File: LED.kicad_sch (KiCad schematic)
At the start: 15 parts

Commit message: error check passed
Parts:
- RFB_730: value 0.1 Ohm -> 0.13 Ohm
- RFB_850: value 0.1 Ohm -> 0.13 Ohm; symbol C_Small_US:C_Small_US -> R_Small_US:R_Small_US
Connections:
- net VLED renamed VBAT_SYSTEM
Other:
- moved on the sheet: D_850

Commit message: placement finished on PCB
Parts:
- C730_BYP1, C850_BYP1, CSLOPE_730, CSLOPE_850, C_TEMP1: footprint LightFusion:C_0402_1005Metric -> LightFusion:C_0603_1608Metric
- R_TEMP_ALERT1: footprint LightFusion:R_0402_1005Metric -> LightFusion:R_0603_1608Metric
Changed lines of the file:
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@@
 		(property "Value" "10 nF"
 			(at 223.52 100.4569 0)
-			(show_name no)
-			(do_not_autoplace no)
-			(effects
-				(font
-					(size 1.27 1.27)
-				)
-				(justify left)
-			)
-		)
-		(property "Footprint" "LightFusion:C_0402_1005Metric"
+			(hide yes)
+			(show_name no)
+			(do_not_autoplace no)
+			(effects
+				(font
+					(size 1.27 1.27)
+				)
+				(justify left)
+			)
+		)
+		(property "Footprint" "LightFusion:C_0603_1608Metric"
 			(at 220.98 99.06 0)
 			(hide yes)
@@
 		(property "Value" "10 nF"
 			(at 133.35 99.1869 0)
-			(show_name no)
-			(do_not_autoplace no)
-			(effects
-				(font
-					(size 1.27 1.27)
-				)
-				(justify left)
-			)
-		)
-		(property "Footprint" "LightFusion:C_0402_1005Metric"
+			(hide yes)
+			(show_name no)
+			(do_not_autoplace no)
+			(effects
+				(font
+					(size 1.27 1.27)
+				)
+				(justify left)
+			)
+		)
+		(property "Footprint" "LightFusion:C_0603_1608Metric"
 			(at 130.81 97.79 0)
 			(hide yes)
@@
 			)
 		)
-		(property "Footprint" "LightFusion:C_0402_1005Metric"
+		(property "Footprint" "LightFusion:C_0603_1608Metric"
 			(at 137.16 124.46 0)
 			(hide yes)
@@
 		(property "Value" "4.7 uF"
 			(at 209.55 64.8969 0)
+			(hide yes)
 			(show_name no)
 			(do_not_autoplace no)
@@
 		(property "Value" "4.7 uF"
 			(at 97.79 64.8969 0)
+			(hide yes)
 			(show_name no)
 			(do_not_autoplace no)
@@
 			)
 		)
-		(property "Footprint" "LightFusion:R_0402_1005Metric"
+		(property "Footprint" "LightFusion:R_0603_1608Metric"
 			(at 125.73 114.3 0)
 			(hide yes)
@@
 		(property "Value" "100 nF"
 			(at 85.09 64.8969 0)
-			(show_name no)
-			(do_not_autoplace no)
-			(effects
-				(font
-					(size 1.27 1.27)
-				)
-				(justify left)
-			)
-		)
-		(property "Footprint" "LightFusion:C_0402_1005Metric"
+			(hide yes)
+			(show_name no)
+			(do_not_autoplace no)
+			(effects
+				(font
+					(size 1.27 1.27)
+				)
+				(justify left)
+			)
+		)
+		(property "Footprint" "LightFusion:C_0603_1608Metric"
 			(at 82.55 63.5 0)
 			(hide yes)
@@
 		(property "Value" "100 nF"
 			(at 196.85 64.8969 0)
-			(show_name no)
-			(do_not_autoplace no)
-			(effects
-				(font
-					(size 1.27 1.27)
-				)
-				(justify left)
-			)
-		)
-		(property "Footprint" "LightFusion:C_0402_1005Metric"
+			(hide yes)
+			(show_name no)
+			(do_not_autoplace no)
+			(effects
+				(font
+					(size 1.27 1.27)
+				)
+				(justify left)
+			)
+		)
+		(property "Footprint" "LightFusion:C_0603_1608Metric"
 			(at 194.31 63.5 0)
 			(hide yes)

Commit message: final verifications
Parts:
- D_730, D_850: now not fitted
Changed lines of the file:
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@@
 		(fields_autoplaced yes)
 		(property "Reference" "CSLOPE_850"
-			(at 223.52 97.9169 0)
+			(at 223.52 99.1869 0)
 			(show_name no)
 			(do_not_autoplace no)
@@
 		(fields_autoplaced yes)
 		(property "Reference" "CSLOPE_730"
-			(at 133.35 96.6469 0)
+			(at 133.35 97.9169 0)
 			(show_name no)
 			(do_not_autoplace no)
@@
 		(on_board yes)
 		(in_pos_files yes)
-		(dnp no)
+		(dnp yes)
 		(fields_autoplaced yes)
 		(property "Reference" "D_850"
-			(at 257.81 60.9599 0)
+			(at 257.81 62.2299 0)
 			(show_name no)
 			(do_not_autoplace no)
@@
 	)
 	(symbol
-		(lib_name "STCS1APHR_FIXED_1")
 		(lib_id "STCS1APHR:STCS1APHR_FIXED")
 		(at 88.9 80.01 0)
@@
 		(fields_autoplaced yes)
 		(property "Reference" "C850_BULK1"
-			(at 209.55 62.3569 0)
+			(at 209.55 63.6269 0)
 			(show_name no)
 			(do_not_autoplace no)
@@
 		(fields_autoplaced yes)
 		(property "Reference" "C730_BULK1"
-			(at 97.79 62.3569 0)
+			(at 97.79 63.6269 0)
 			(show_name no)
 			(do_not_autoplace no)
@@
 		(on_board yes)
 		(in_pos_files yes)
-		(dnp no)
+		(dnp yes)
 		(fields_autoplaced yes)
 		(property "Reference" "D_730"
@@
 		(fields_autoplaced yes)
 		(property "Reference" "C730_BYP1"
-			(at 85.09 62.3569 0)
+			(at 85.09 63.6269 0)
 			(show_name no)
 			(do_not_autoplace no)
@@
 		(fields_autoplaced yes)
 		(property "Reference" "C850_BYP1"
-			(at 196.85 62.3569 0)
-			(show_name no)
-			(do_not_autoplace no)
+			(at 196.85 63.6269 0)
+			(show_name no)
+			(do_not_autoplace no)

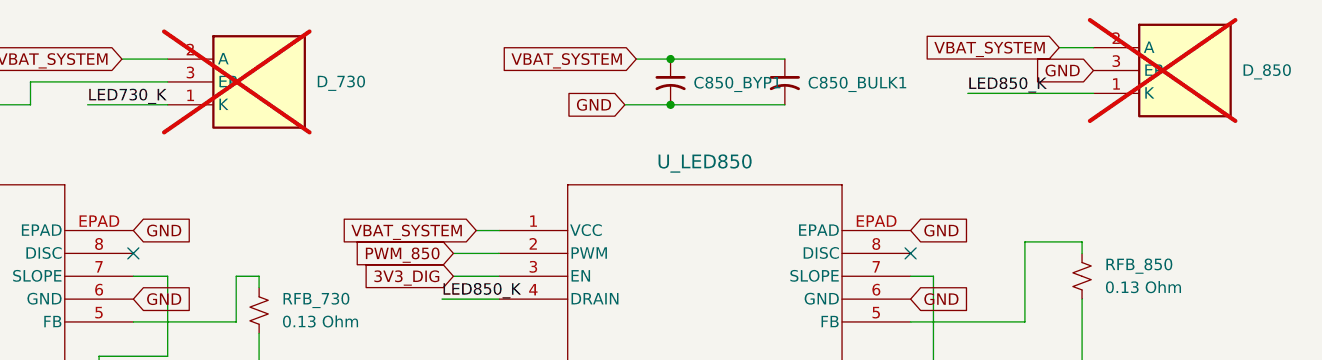
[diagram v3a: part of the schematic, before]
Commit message: Add new electrode positions to positions.csv
- Added D_730 and D_850 at specified coordinates on the bottom layer.
- Introduced E_EEG1, E_EEG2, and E_EEG3 at new coordinates on the bottom layer.
- Included STIM_E_N1 and STIM_E_P1 at new coordinates on the bottom layer.
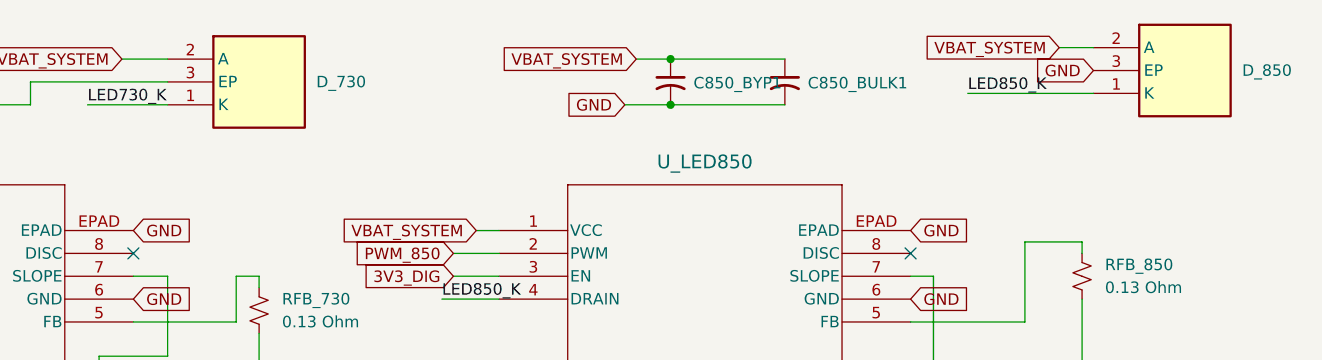
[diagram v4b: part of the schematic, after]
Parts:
- D_730, D_850: now fitted
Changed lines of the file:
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@@
 		(on_board yes)
 		(in_pos_files yes)
-		(dnp yes)
+		(dnp no)
 		(fields_autoplaced yes)
 		(property "Reference" "D_850"
@@
 		(on_board yes)
 		(in_pos_files yes)
-		(dnp yes)
+		(dnp no)
 		(fields_autoplaced yes)
 		(property "Reference" "D_730"

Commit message: final version with bom and placement
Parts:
- renumbered C730_BULK1 to C26, C730_BYP1 to C27, C850_BULK1 to C28, C850_BYP1 to C29, CSLOPE_730 to C30, CSLOPE_850 to C31, C_TEMP1 to C32, D_730 to D1, D_850 to D2, RFB_730 to R25, RFB_850 to R26, R_TEMP_ALERT1 to R27, U_LED730 to U6, U_LED850 to U7, U_TEMP1 to U8
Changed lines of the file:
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@@
 		(dnp no)
 		(fields_autoplaced yes)
-		(property "Reference" "CSLOPE_850"
+		(property "Reference" "C31"
 			(at 223.52 99.1869 0)
 			(show_name no)
@@
 			(project "LightFusion"
 				(path "/1aacc45f-6fcc-4559-bec0-55c6f50555c1/4f6c1d6e-1436-41bd-90e8-4017848590b3"
-					(reference "CSLOPE_850")
+					(reference "C31")
 					(unit 1)
 				)
@@
 		(dnp no)
 		(fields_autoplaced yes)
-		(property "Reference" "CSLOPE_730"
+		(property "Reference" "C30"
 			(at 133.35 97.9169 0)
 			(show_name no)
@@
 			(project "LightFusion"
 				(path "/1aacc45f-6fcc-4559-bec0-55c6f50555c1/4f6c1d6e-1436-41bd-90e8-4017848590b3"
-					(reference "CSLOPE_730")
+					(reference "C30")
 					(unit 1)
 				)
@@
 		(dnp no)
 		(fields_autoplaced yes)
-		(property "Reference" "D_850"
+		(property "Reference" "D2"
 			(at 257.81 62.2299 0)
 			(show_name no)
@@
 			(project "LightFusion"
 				(path "/1aacc45f-6fcc-4559-bec0-55c6f50555c1/4f6c1d6e-1436-41bd-90e8-4017848590b3"
-					(reference "D_850")
+					(reference "D2")
 					(unit 1)
 				)
@@
 		(dnp no)
 		(fields_autoplaced yes)
-		(property "Reference" "RFB_730"
+		(property "Reference" "R25"
 			(at 151.13 87.6299 0)
 			(show_name no)
@@
 		(property "Value" "0.13 Ohm"
 			(at 151.13 90.1699 0)
+			(hide yes)
 			(show_name no)
 			(do_not_autoplace no)
@@
 			(project "LightFusion"
 				(path "/1aacc45f-6fcc-4559-bec0-55c6f50555c1/4f6c1d6e-1436-41bd-90e8-4017848590b3"
-					(reference "RFB_730")
+					(reference "R25")
 					(unit 1)
 				)
@@
 		(dnp no)
 		(fields_autoplaced yes)
-		(property "Reference" "U_LED730"
+		(property "Reference" "U6"
 			(at 111.76 72.39 0)
 			(show_name no)
@@
 			(project "LightFusion"
 				(path "/1aacc45f-6fcc-4559-bec0-55c6f50555c1/4f6c1d6e-1436-41bd-90e8-4017848590b3"
-					(reference "U_LED730")
+					(reference "U6")
 					(unit 1)
 				)
@@
 		(dnp no)
 		(fields_autoplaced yes)
-		(property "Reference" "C_TEMP1"
+		(property "Reference" "C32"
 			(at 139.7 123.3169 0)
 			(show_name no)
@@
 		(property "Value" "10 nF"
 			(at 139.7 125.8569 0)
+			(hide yes)
 			(show_name no)
 			(do_not_autoplace no)
@@
 			(project "LightFusion"
 				(path "/1aacc45f-6fcc-4559-bec0-55c6f50555c1/4f6c1d6e-1436-41bd-90e8-4017848590b3"
-					(reference "C_TEMP1")
+					(reference "C32")
 					(unit 1)
 				)
@@
 		(in_pos_files yes)
 		(dnp no)
-		(fields_autoplaced yes)
-		(property "Reference" "C850_BULK1"
-			(at 209.55 63.6269 0)
+		(property "Reference" "C28"
+			(at 208.28 63.5 0)
 			(show_name no)
 			(do_not_autoplace no)
@@
 			(project "LightFusion"
 				(path "/1aacc45f-6fcc-4559-bec0-55c6f50555c1/4f6c1d6e-1436-41bd-90e8-4017848590b3"
-					(reference "C850_BULK1")
+					(reference "C28")
 					(unit 1)
 				)
@@
 		(dnp no)
 		(fields_autoplaced yes)
-		(property "Reference" "C730_BULK1"
+		(property "Reference" "C26"
 			(at 97.79 63.6269 0)
 			(show_name no)
@@
 			(project "LightFusion"
 				(path "/1aacc45f-6fcc-4559-bec0-55c6f50555c1/4f6c1d6e-1436-41bd-90e8-4017848590b3"
-					(reference "C730_BULK1")
+					(reference "C26")
 					(unit 1)
 				)
@@
 		(in_pos_files yes)
 		(dnp no)
-		(fields_autoplaced yes)
-		(property "Reference" "R_TEMP_ALERT1"
-			(at 128.27 113.0299 0)
+		(property "Reference" "R27"
+			(at 127 113.03 0)
 			(show_name no)
 			(do_not_autoplace no)
@@
 		(property "Value" "4.7 kOhm"
 			(at 128.27 115.5699 0)
+			(hide yes)
 			(show_name no)
 			(do_not_autoplace no)
@@
 			(project "LightFusion"
 				(path "/1aacc45f-6fcc-4559-bec0-55c6f50555c1/4f6c1d6e-1436-41bd-90e8-4017848590b3"
-					(reference "R_TEMP_ALERT1")
+					(reference "R27")
 					(unit 1)
 				)
@@
 		(in_pos_files yes)
 		(dnp no)
-		(fields_autoplaced yes)
-		(property "Reference" "RFB_850"
-			(at 242.57 83.8199 0)
+		(property "Reference" "R26"
+			(at 241.3 83.82 0)
 			(show_name no)
 			(do_not_autoplace no)
@@
 		(property "Value" "0.13 Ohm"
 			(at 242.57 86.3599 0)
+			(hide yes)
 			(show_name no)
 			(do_not_autoplace no)
@@
 			(project "LightFusion"
 				(path "/1aacc45f-6fcc-4559-bec0-55c6f50555c1/4f6c1d6e-1436-41bd-90e8-4017848590b3"
-					(reference "RFB_850")
+					(reference "R26")
 					(unit 1)
 				)
@@
 		(dnp no)
 		(fields_autoplaced yes)
-		(property "Reference" "D_730"
+		(property "Reference" "D1"
 			(at 154.94 63.4999 0)
 			(show_name no)
@@
 			(project "LightFusion"
 				(path "/1aacc45f-6fcc-4559-bec0-55c6f50555c1/4f6c1d6e-1436-41bd-90e8-4017848590b3"
-					(reference "D_730")
+					(reference "D1")
 					(unit 1)
 				)
@@
 		(dnp no)
 		(fields_autoplaced yes)
-		(property "Reference" "C730_BYP1"
+		(property "Reference" "C27"
 			(at 85.09 63.6269 0)
 			(show_name no)
@@
 			(project "LightFusion"
 				(path "/1aacc45f-6fcc-4559-bec0-55c6f50555c1/4f6c1d6e-1436-41bd-90e8-4017848590b3"
-					(reference "C730_BYP1")
+					(reference "C27")
 					(unit 1)
 				)
@@
 		(in_pos_files yes)
 		(dnp no)
-		(property "Reference" "U_TEMP1"
+		(property "Reference" "U8"
 			(at 96.52 116.84 0)
 			(show_name no)
@@
 			(project "LightFusion"
 				(path "/1aacc45f-6fcc-4559-bec0-55c6f50555c1/4f6c1d6e-1436-41bd-90e8-4017848590b3"
-					(reference "U_TEMP1")
+					(reference "U8")
 					(unit 1)
 				)
@@
 		(dnp no)
 		(fields_autoplaced yes)
-		(property "Reference" "C850_BYP1"
+		(property "Reference" "C29"
 			(at 196.85 63.6269 0)
 			(show_name no)
@@
 			(project "LightFusion"
 				(path "/1aacc45f-6fcc-4559-bec0-55c6f50555c1/4f6c1d6e-1436-41bd-90e8-4017848590b3"
-					(reference "C850_BYP1")
+					(reference "C29")
 					(unit 1)
 				)
@@
 		(dnp no)
 		(fields_autoplaced yes)
-		(property "Reference" "U_LED850"
+		(property "Reference" "U7"
 			(at 198.12 72.39 0)
 			(show_name no)
@@
 			(project "LightFusion"
 				(path "/1aacc45f-6fcc-4559-bec0-55c6f50555c1/4f6c1d6e-1436-41bd-90e8-4017848590b3"
-					(reference "U_LED850")
-					(unit 1)
-				)
+					(reference "U7")
+					(unit 1)
+				)
